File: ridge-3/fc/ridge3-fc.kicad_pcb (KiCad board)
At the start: 6 copper layers, 36 x 36 mm, 118 parts, among them Y1 8MHz, Y2 27MHz

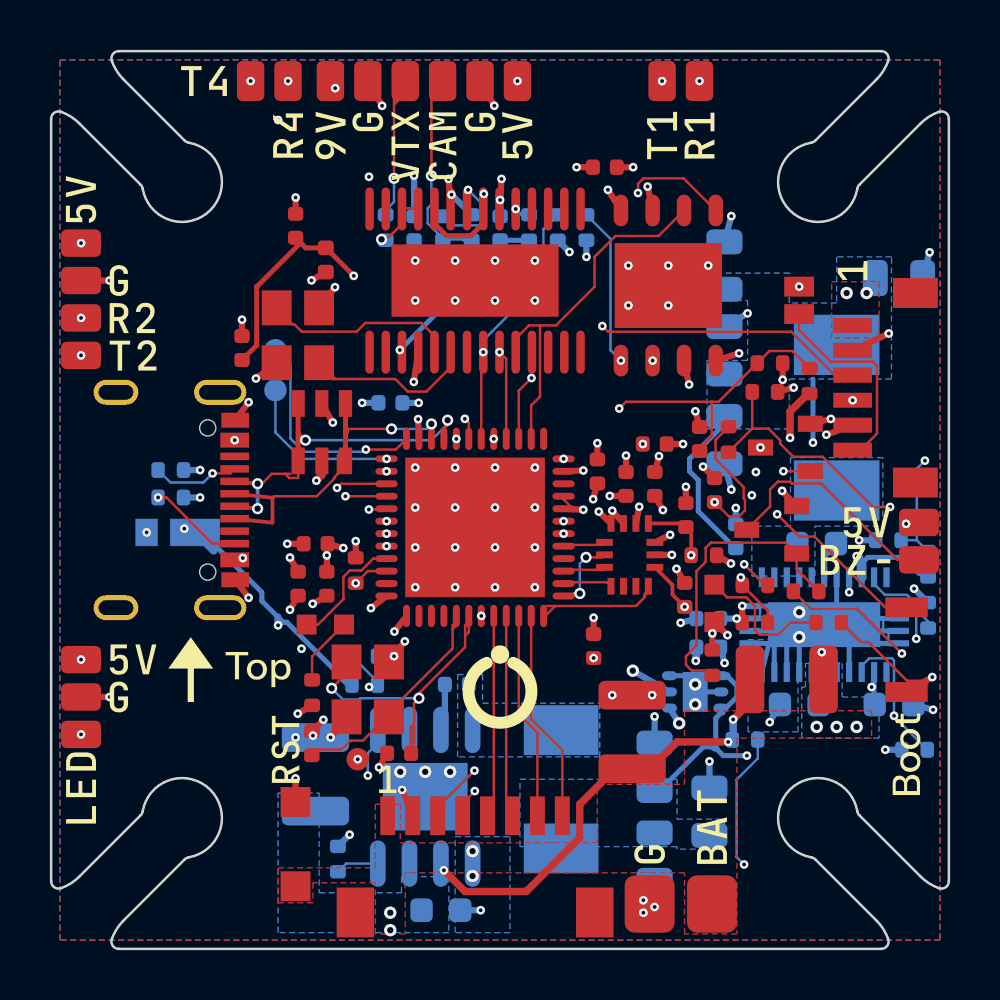
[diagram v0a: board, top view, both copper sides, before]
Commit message: FC gyro: TDK ICM-45686, BMI270 as second source; FC re-routed
- circuit.py/parts.py: U_IMU is the ICM-45686 (LCSC C22459454, DigiKey
  1428-ICM-45686CT-ND) on the same LGA-14 pads.  Every pin either chip
  leaves unused is open, the first choice in both datasheets: 2/3 (aux),
  9 (INT2/FSYNC: TDK "NC or VDDIO", Bosch "do not connect"), and now
  10/11 (TDK RESV pull-ups; Bosch OCSB/OSDO "DNC").  Pin 7 stays GND (the
  BMI270's GND).  The ICM-42688-P no longer fits (it wants pin 9 at GND).
- Betaflight: RIDGE3 is the ICM-45686 build (CW0, 6.4 kHz gyro, PID
  denom 2 = 3.2 kHz); RIDGE3_BMI replaces RIDGE3_ICM (BMI270, CW270).
  Both hexes rebuilt; hashes in firmware/README.md.
- pipeline.py: a board routed whole (the FC) that still has nets open
  after the repairs is routed again under three other Freerouting costs
  in parallel; the fewest open wins, first of equals.  The FC now routes
  at via_costs 30 (defaults left BEEPER open).  DRC 0/0/0.
- panel.py: a straight track counts as an edge feature only over the
  stretch inside the edge band, not its bounding box (a diagonal +9V
  track blocked the FC's second tab).  ESC panel tabs move to 8.9 mm.
- verify.py: IMU pad, build and BOM checks for the new part; 206 pass.
- README: ICM-45686, costs of 29 Sept 2026 (stack $84.48 / $57.12 /
  $53.60 at 1 / 100 / 1,000), gyro stock row; parts_final.md addendum.

Co-Authored-By: Claude Opus 5.5 <noreply@anthropic.com>
Claude-Session: https://claude.ai/code/session_01MaVFAzoExts7u2gmCraXFC
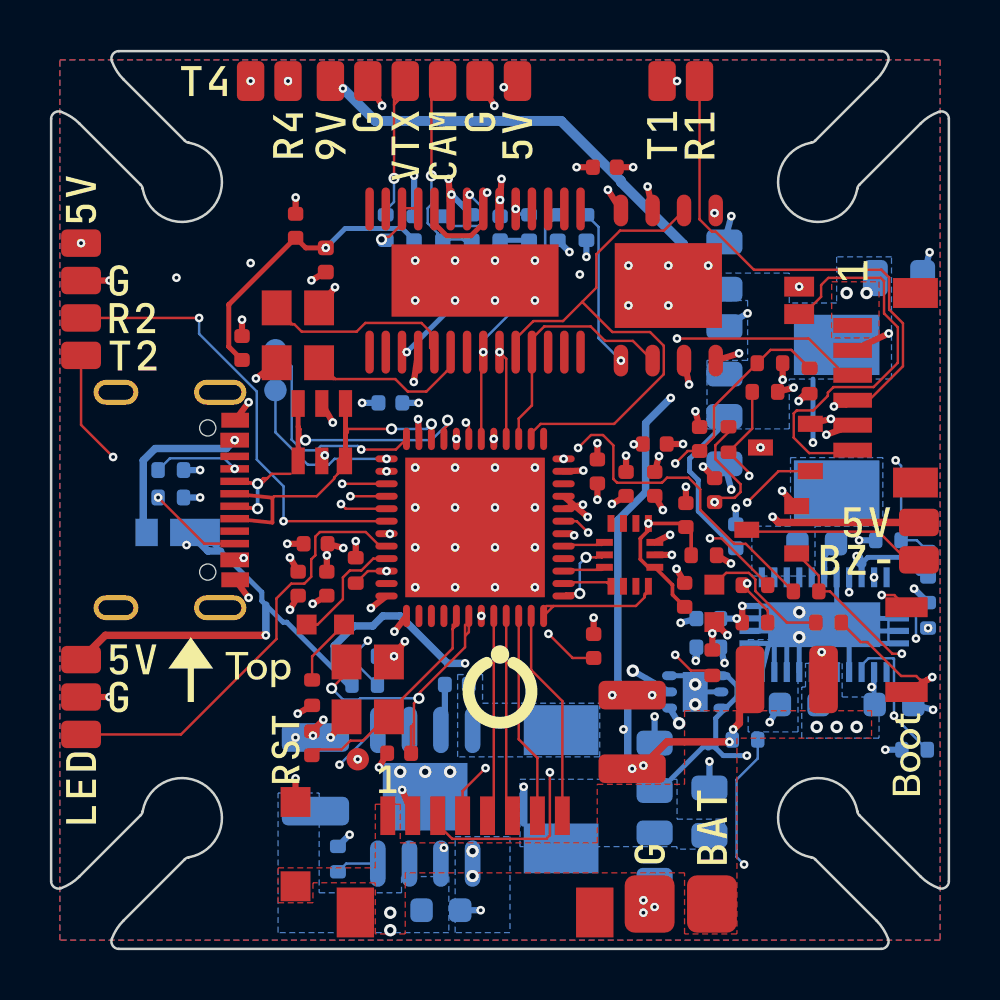
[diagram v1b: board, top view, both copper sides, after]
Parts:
- U_IMU: value BMI270 -> ICM-45686
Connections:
- U_IMU pad 10: GND -> (no net)
- U_IMU pad 11: GND -> (no net)
- U_IMU pad 9: GND -> (no net)
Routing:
- net BEEPER: track 34.1 -> 21.3 mm
- net HD_SBUS: track 8.34 -> 16.6 mm
- net CUR: track 35.5 -> 27.6 mm
- net +9V: track 43.3 -> 35.5 mm, vias 6 -> 5
- net VBAT: track 28.3 -> 35.9 mm, vias 10 -> 13
- net SPI2_SCK: track 14.8 -> 21.9 mm
- net UART2_RX: track 37.5 -> 43.0 mm
- net BEEPER_G: track 12.1 -> 17.5 mm, vias 0 -> 2
- net UART1_RX: track 31.9 -> 37.3 mm, vias 3 -> 2
- net VTX_OFF: track 20.0 -> 16.4 mm, vias 3 -> 2
- net BUCK5_FB: track 6.53 -> 10.0 mm
- net BOOT0: track 26.2 -> 23.1 mm
- net USB_VBUS: track 13.8 -> 16.8 mm, vias 4 -> 3
- net ADC_VBAT: track 16.5 -> 14.1 mm
- net LED_STRIP: track 15.4 -> 17.6 mm, vias 2 -> 0
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
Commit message: FC: rerouted with Freerouting 1.9 to DRC 0; fixed parts kept apart
The full FC reroute ended at 8 DRC errors, all from parts that fixed()
places exactly where the tables say: the packer keeps the parts it moves
clear, but never checks fixed parts against each other.
- The 3.3 V buck's input capacitor moves 0.55 mm right. Its 5 V pad sat
  on the USB-C's front shell tab, a plated hole with copper on the bottom
  (a short). The buck's ground pour widens behind the switch node to take
  the capacitor's moved pad.
- The 3.3 V output capacitors sit in front of the inductor's courtyard.
- The battery lead's clamp moves outboard and the video input's clamp
  forward, clear of the 5 V BEC IC and the battery pads.
- The 9 V BEC's RT resistor stays in line with its pin, past the end of
  the IC's courtyard.
- build_placed now checks every placement the way the DRC will (courtyards
  overlapping or touching on one side, a hole in another part's courtyard)
  and stops the build there, before an hour of routing.

DRC 0 errors, 0 warnings, 0 unconnected; netlist, BOM and CPL gates pass.
The board, production files, renders and STEP are regenerated.

Co-Authored-By: Claude Opus 5.5 <noreply@anthropic.com>
Claude-Session: https://claude.ai/code/session_01MaVFAzoExts7u2gmCraXFC
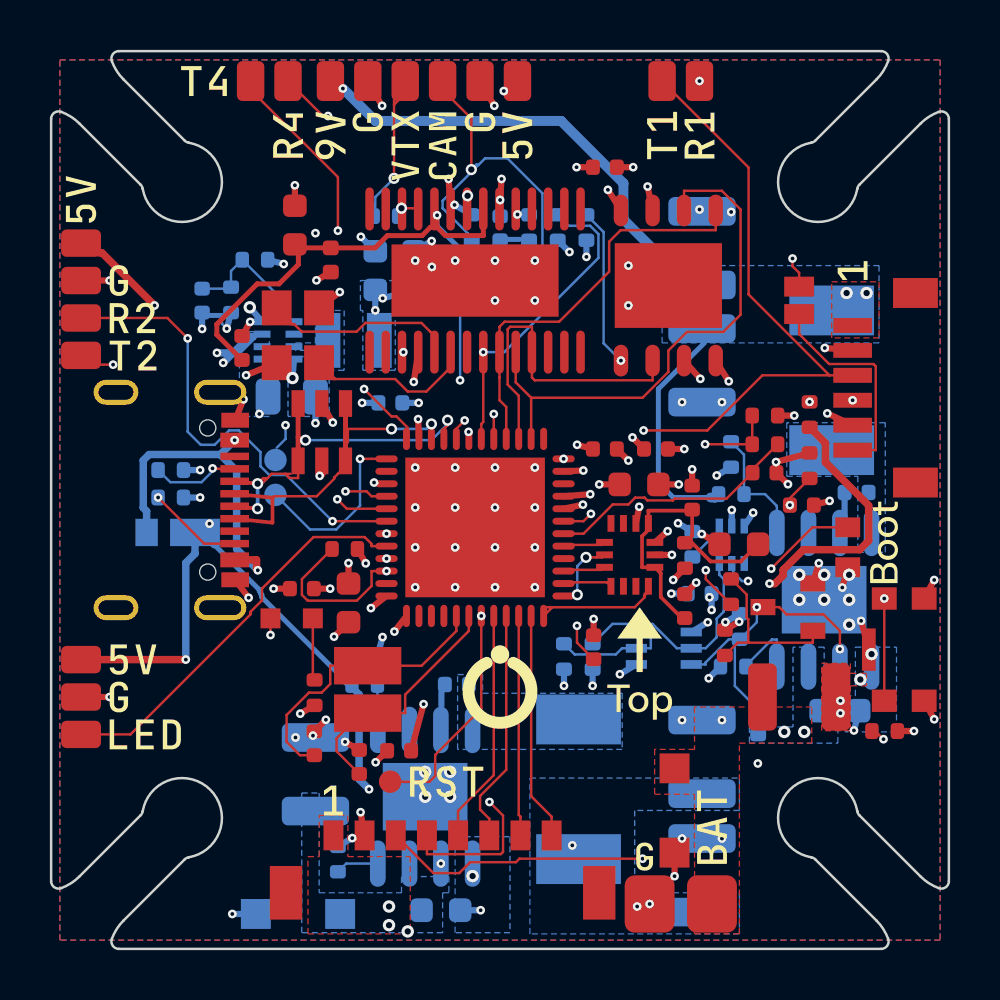
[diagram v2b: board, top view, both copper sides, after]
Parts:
- removed C37, C38, C39: 100nF, C_0402_1005Metric
- removed the J_ESC at (99.0, 114.6)
- removed the LED_PWR at (108.6, 104.1)
- removed the LED_STAT at (93.0, 105.0)
- removed the L_5V at (102.5, 111.6)
- removed the L_9V at (113.5, 96.7)
- removed P_BZ+, P_BZ-: PAD_SIG, PAD_SIG
- removed Q_BZ: AO3400A, SOT-23-3_L2.9-W1.3-P1.90-LS2.4-BR
- removed the SW_BOOT at (116.3, 106.0)
- removed U_LDO: TLV76733 3.3V, WSON-6_L2.0-W2.0-P0.65-TL-EP
- added D_TVS9: SMF33A, SMF_L2.8-W1.8-LS3.7-RD, F.Cu at (107.0, 112.5)
- added J_ESC: Micro-Lock Plus 8P RA, CONN-SMD_8P-P1.25_5055670871, F.Cu at (97.7, 114.6)
- added LED_PWR: RED, LED0603-RD_1, F.Cu at (113.9, 101.9)
- added LED_STAT: BLUE, LED0603-R-RD_BLUE, F.Cu at (91.6, 104.7)
- added L_3V3: 0.47uH, IND-SMD_L2.5-W2.0_TFM252012ALMA2R2MTAA, B.Cu at (94.1, 93.6)
- added L_5V: 15uH, IND-SMD_L7.1-W6.5_SPM6530T, B.Cu at (103.2, 111.6)
- added L_9V: 15uH, IND-SMD_L7.1-W6.5_SPM6530T, B.Cu at (113.3, 95.2)
- added Q_TSW: BSS138DW, SC-70-6_L2.0-W1.3-P0.65-LS2.1-BL, B.Cu at (106.6, 105.9)
- added R28: 5.1k, R_0402_1005Metric, B.Cu at (86.8, 99.9)
- added R29: 1k, R_0402_1005Metric, F.Cu at (115.4, 109.3)
- added R30: 330R, R_0402_1005Metric, F.Cu at (92.6, 107.7)
- added SW_BOOT: BOOT, SW-SMD_5P-L4.2-W2.8-P1.60-LS4.6-TR, F.Cu at (115.9, 106.0)
- added U_BUCK3: TPS628501, SOT-583-8_L2.1-W1.6-P0.50-LS1.6-BL, B.Cu at (91.1, 93.6)
- added U_TSW: TMP390A2, SOT-563_L1.6-W1.2-P0.50-LS1.6-BR, B.Cu at (109.3, 101.8)
- C1: value 10uF -> 100nF; footprint C_1210_3225Metric -> C_0402_1005Metric
- C10: value 10uF -> 100nF; footprint C_1210_3225Metric -> C_0402_1005Metric; moved to B.Cu
- C11, C5: footprint C_0603_1608Metric -> C_0402_1005Metric
- C12: value 470nF -> 22uF; footprint C_0603_1608Metric -> C_1210_3225Metric
- C13: value 2.2uF -> 22uF; footprint C_0603_1608Metric -> C_1210_3225Metric
- C14: value 1uF -> 10uF; footprint C_0402_1005Metric -> C_0805_2012Metric
- C15, C16: value 22uF -> 4.7uF; footprint C_0805_2012Metric -> C_0603_1608Metric
- C17: value 22uF -> 10pF; footprint C_0805_2012Metric -> C_0402_1005Metric
- C18: value 22uF -> 100nF; footprint C_0805_2012Metric -> C_0402_1005Metric; moved to F.Cu
- C19: value 1uF -> 100nF; moved to F.Cu
- C20, C31: value 4.7uF -> 100nF
- C23: value 100nF -> 1uF; footprint C_0402_1005Metric -> C_0603_1608Metric; moved to F.Cu
- C24, C28, C32: value 100nF -> 4.7uF; footprint C_0402_1005Metric -> C_0603_1608Metric
- C26: value 1uF -> 10pF
- C27: value 4.7uF -> 10pF
- C29, C30: value 12pF -> 100nF
- C3: value 100nF -> 10uF; footprint C_0402_1005Metric -> C_1210_3225Metric; moved to B.Cu
- C34, C36, D_TVS: moved to B.Cu
- C35: value 4.7uF -> 100nF; moved to B.Cu
- C4: value 10uF -> 100nF; footprint C_1210_3225Metric -> C_0603_1608Metric
- C6: value 100nF -> 22uF; footprint C_0402_1005Metric -> C_1210_3225Metric
- C7: footprint C_0805_2012Metric -> C_1210_3225Metric
- C8: value 22uF -> 10uF; footprint C_0805_2012Metric -> C_1210_3225Metric; moved to F.Cu
- C9: value 22uF -> 100nF; footprint C_0805_2012Metric -> C_0603_1608Metric
- R13: value 100k -> 121k
- R14: value 12.4k -> 10k
- R15: value 10k -> 100k; moved to B.Cu
- R16: value 10R -> 100k; moved to B.Cu
- R17: value 10k -> 12.4k
- R18: value 10k -> 100k
- R19: value 10k -> 22.1k
- R20: value 75R -> 3.3k; moved to F.Cu
- R21: value 75R -> 10R; moved to F.Cu
- R22, R23: value 5.1k -> 10k
- R24: value 1k -> 10k; moved to B.Cu
- R25: value 330R -> 75R; moved to B.Cu
- R26: value 100R -> 75R; moved to B.Cu
- R27: value 10k -> 5.1k; moved to B.Cu
- R5: value 25.5k -> 57.6k
- R8: value 24.3k -> 57.6k
- U_BUCK9: value LM76003 -> LMR38020F; footprint WQFN-30_L6.0-W4.0-P0.50-BL-EP -> ESOP-8_L4.9-W3.9-P1.27-LS6.0-BL-EP-1
- U_FLASH: value W25Q128JVPIM -> S25FL128LAGNFM010
- U_IMU: value ICM-45686 -> IIM-42652
- Y1: footprint CRYSTAL-SMD_4P-L3.2-W2.5-BL -> OSC-SMD_2P-L3.2-W2.5
- moved C18 27.6 mm to (96.0, 110.1), turned to 180 degrees
- moved R27 23.0 mm to (86.8, 98.8), turned to 0 degrees
- moved R26 22.6 mm to (95.4, 88.6), turned to 180 degrees
- moved C32 21.5 mm to (91.8, 89.0)
- moved C17 21.0 mm to (88.1, 92.0)
- moved C3 20.4 mm to (92.6, 111.0)
- moved R24 19.9 mm to (101.2, 89.1), turned to 90 degrees
- moved C13 19.9 mm to (108.1, 89.9), turned to 90 degrees
- moved R25 19.7 mm to (98.9, 89.1)
- moved R22 19.3 mm to (103.5, 89.1), turned to 90 degrees
- moved R23 18.9 mm to (102.3, 89.1), turned to 90 degrees
- moved C14 18.7 mm to (91.7, 95.8), turned to 0 degrees
- moved R21 17.8 mm to (107.4, 102.2)
- moved C26 17.2 mm to (92.6, 109.8)
- moved C33 17.0 mm to (89.7, 93.9), turned to 90 degrees
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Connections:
- C1 pad 1: VBAT -> ADC_CURR
- C10 pad 1: VBAT -> BUCK9_CB
- C10 pad 2: GND -> BUCK9_SW
- C11 pad 1: VBAT -> +3V3
- C12 pad 1: BUCK9_CB -> +9V
- C12 pad 2: BUCK9_SW -> GND
- C13 pad 1: BUCK9_VCC -> +9V
- C14 pad 1: +9V -> +5V
- C15 pad 1: +9V -> +3V3
- C16 pad 1: +9V -> +3V3
- C17 pad 1: +9V -> +3V3
- C17 pad 2: GND -> BUCK3_FB
- C18 pad 1: +9V -> +3V3
- C19 pad 1: +5V -> +3V3
- C2 pad 1: ADC_CURR -> ADC_VBAT
- C25 pad 1: +3V3 -> NRST
- C26 pad 1: +3V3 -> HSE_IN
- C27 pad 1: +3V3 -> HSE_OUT
- C28 pad 1: NRST -> +3V3_GYRO
- C29 pad 1: HSE_IN -> +3V3_GYRO
- C3 pad 1: ADC_VBAT -> VBAT
- C30 pad 1: HSE_OUT -> +3V3_GYRO
- C31 pad 1: +3V3_GYRO -> +3V3
- C32 pad 1: +3V3_GYRO -> +3V3_OSD
- C33 pad 1: +3V3_GYRO -> +3V3_OSD
- C34 pad 1: +3V3 -> +3V3_OSD
- C36 pad 1: +3V3_OSD -> CAM_VIDEO
- C36 pad 2: GND -> OSD_VIN
- C5 pad 1: VBAT -> BUCK5_CB
- C5 pad 2: GND -> BUCK5_SW
- C6 pad 1: BUCK5_CB -> +5V
- C6 pad 2: BUCK5_SW -> GND
- C8 pad 1: +5V -> VBAT_VTX
- C9 pad 1: +5V -> VBAT_VTX
- P_BAT pad 1: VBAT -> VBAT_VTX
- R13 pad 1: +9V -> VTX_TSET
- R13 pad 2: BUCK9_FB -> GND
- R14 pad 1: BUCK9_FB -> +3V3
- R14 pad 2: GND -> VTX_COOL
- R15 pad 1: BOOT0 -> +3V3
- R15 pad 2: GND -> VTX_HOT_G
- R16 pad 1: +3V3 -> +9V
- R16 pad 2: +3V3_GYRO -> BUCK9_FB
- R17 pad 1: +3V3 -> BUCK9_FB
- R17 pad 2: FLASH_CS -> GND
- R18 pad 1: +3V3_OSD -> +3V3
- R18 pad 2: OSD_RST -> BUCK3_FB
- R19 pad 1: +3V3 -> BUCK3_FB
- R19 pad 2: OSD_CS -> GND
- R20 pad 1: CAM_VIDEO -> BOOT0
- R21 pad 1: OSD_VOUT -> +3V3
- R21 pad 2: VTX_VIDEO -> +3V3_GYRO
- R22 pad 1: USB_CC1 -> +3V3
- R22 pad 2: GND -> FLASH_CS
- R23 pad 1: USB_CC2 -> +3V3
- R23 pad 2: GND -> OSD_CS
- R24 pad 1: +3V3 -> +3V3_OSD
- R24 pad 2: LED_PWR_A -> OSD_RST
- R25 pad 1: +3V3 -> CAM_VIDEO
- R25 pad 2: LED0_A -> GND
- R26 pad 1: BEEPER -> OSD_VOUT
- R26 pad 2: BEEPER_G -> VTX_VIDEO
- R27 pad 1: BEEPER_G -> USB_CC1
- R9 pad 1: VBAT -> VBAT_VTX
- U_BUCK9 pad 1: BUCK9_SW -> GND
- U_BUCK9 pad 2: BUCK9_SW -> BUCK9_EN
- U_BUCK9 pad 3: BUCK9_SW -> VBAT_VTX
- U_BUCK9 pad 4: BUCK9_SW -> BUCK9_RT
- U_BUCK9 pad 5: BUCK9_SW -> BUCK9_FB
- U_BUCK9 pad 6: BUCK9_CB -> (no net)
- U_BUCK9 pad 7: GND -> BUCK9_CB
- U_BUCK9 pad 8: BUCK9_VCC -> BUCK9_SW
- U_BUCK9 pad 9: +9V -> GND
- U_FC pad 38: BEEPER -> (no net)
- U_IMU pad 9: (no net) -> GND
- Y1 pad 2: GND -> HSE_OUT
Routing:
- net +5V: track 94.1 -> 64.0 mm, vias 11 -> 10
- net BUCK9_EN: track 35.2 -> 12.4 mm, vias 3 -> 2
- net BEEPER: track 21.3 -> 0.00 mm, vias 2 -> 0
- net GND: track 80.9 -> 61.8 mm, vias 115 -> 122
- net BEEPER_G: track 17.5 -> 0.00 mm, vias 2 -> 0
- net CAM_VIDEO: track 8.07 -> 18.1 mm
- net BUCK9_FB: track 14.9 -> 4.91 mm, vias 2 -> 0
- net +9V: track 35.5 -> 26.2 mm, vias 5 -> 3
- net BOOT0: track 23.1 -> 32.2 mm
- net VTX_COOL: track 0.00 -> 9.04 mm
- net LED_PWR_A: track 5.36 -> 13.3 mm, vias 0 -> 2
- net HD_SBUS: track 16.6 -> 8.70 mm
- net OSD_VIN: track 3.78 -> 11.6 mm, vias 1 -> 2
- net BZ-: track 7.40 -> 0.00 mm
- net BUCK5_FB: track 10.0 -> 3.38 mm, vias 2 -> 0
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- added copper zone on B.Cu, net +3V3
- added copper zone on B.Cu, net BUCK3_SW
- added copper zone on B.Cu, net VBAT_VTX
- added copper zone on F.Cu, net VBAT_VTX
